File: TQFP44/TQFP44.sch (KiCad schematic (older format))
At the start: 4 parts, among them J1 Conn_01x22, J2 Conn_01x22, J3 Conn_02x22_Counter_Clockwise, J4 Conn_02x22_Counter_Clockwise

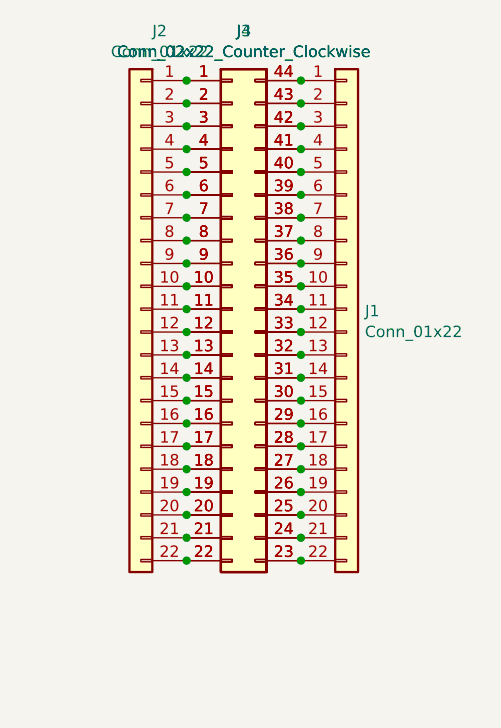
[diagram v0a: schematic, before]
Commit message: SOIC20 and SOIC28 Added
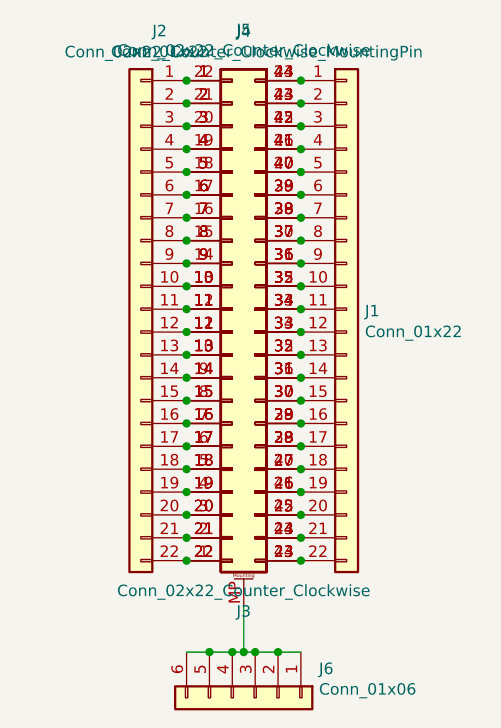
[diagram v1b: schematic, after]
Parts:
- removed J4: Conn_02x22_Counter_Clockwise, Package_DFN_QFN:QFN-44-1EP_7x7mm_P0.5mm_EP5.15x5.15mm_ThermalVias, symbol Connector_Generic:Conn_02x22_Counter_Clockwise
- added J4: Conn_02x22_Counter_Clockwise_MountingPin, Package_DFN_QFN:QFN-44-1EP_7x7mm_P0.5mm_EP5.2x5.2mm, symbol Connector_Generic_MountingPin:Conn_02x22_Counter_Clockwise_MountingPin
- added J5: Conn_02x22_Counter_Clockwise, Package_QFP:TQFP-44_10x10mm_P0.8mm, symbol Connector_Generic:Conn_02x22_Counter_Clockwise
- added J6: Conn_01x06, Connector_PinHeader_2.54mm:PinHeader_1x06_P2.54mm_Horizontal, symbol Connector_Generic:Conn_01x06
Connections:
- net at J1.1 (Pin_1), J3.44 (Pin_44): now also J4.44 (Pin_44), J5.23 (Pin_23)
- net at J1.10 (Pin_10), J3.35 (Pin_35): now also J4.35 (Pin_35), J5.32 (Pin_32)
- net at J1.11 (Pin_11), J3.34 (Pin_34): now also J4.34 (Pin_34), J5.33 (Pin_33)
- net at J1.12 (Pin_12), J3.33 (Pin_33): now also J4.33 (Pin_33), J5.34 (Pin_34)
- net at J1.13 (Pin_13), J3.32 (Pin_32): now also J4.32 (Pin_32), J5.35 (Pin_35)
- net at J1.14 (Pin_14), J3.31 (Pin_31): now also J4.31 (Pin_31), J5.36 (Pin_36)
- net at J1.15 (Pin_15), J3.30 (Pin_30): now also J4.30 (Pin_30), J5.37 (Pin_37)
- net at J1.16 (Pin_16), J3.29 (Pin_29): now also J4.29 (Pin_29), J5.38 (Pin_38)
- net at J1.17 (Pin_17), J3.28 (Pin_28): now also J4.28 (Pin_28), J5.39 (Pin_39)
- net at J1.18 (Pin_18), J3.27 (Pin_27): now also J4.27 (Pin_27), J5.40 (Pin_40)
- net at J1.19 (Pin_19), J3.26 (Pin_26): now also J4.26 (Pin_26), J5.41 (Pin_41)
- net at J1.2 (Pin_2), J3.43 (Pin_43): now also J4.43 (Pin_43), J5.24 (Pin_24)
- net at J1.20 (Pin_20), J3.25 (Pin_25): now also J4.25 (Pin_25), J5.42 (Pin_42)
- net at J1.21 (Pin_21), J3.24 (Pin_24): now also J4.24 (Pin_24), J5.43 (Pin_43)
- net at J1.22 (Pin_22), J3.23 (Pin_23): now also J4.23 (Pin_23), J5.44 (Pin_44)
- net at J1.3 (Pin_3), J3.42 (Pin_42): now also J4.42 (Pin_42), J5.25 (Pin_25)
- net at J1.4 (Pin_4), J3.41 (Pin_41): now also J4.41 (Pin_41), J5.26 (Pin_26)
- net at J1.5 (Pin_5), J3.40 (Pin_40): now also J4.40 (Pin_40), J5.27 (Pin_27)
- net at J1.6 (Pin_6), J3.39 (Pin_39): now also J4.39 (Pin_39), J5.28 (Pin_28)
- net at J1.7 (Pin_7), J3.38 (Pin_38): now also J4.38 (Pin_38), J5.29 (Pin_29)
- net at J1.8 (Pin_8), J3.37 (Pin_37): now also J4.37 (Pin_37), J5.30 (Pin_30)
- net at J1.9 (Pin_9), J3.36 (Pin_36): now also J4.36 (Pin_36), J5.31 (Pin_31)
- net at J2.1 (Pin_1), J3.1 (Pin_1): now also J4.1 (Pin_1), J5.22 (Pin_22)
- net at J2.10 (Pin_10), J3.10 (Pin_10): now also J4.10 (Pin_10), J5.13 (Pin_13)
- net at J2.11 (Pin_11), J3.11 (Pin_11): now also J4.11 (Pin_11), J5.12 (Pin_12)
- net at J2.12 (Pin_12), J3.12 (Pin_12): now also J4.12 (Pin_12), J5.11 (Pin_11)
- net at J2.13 (Pin_13), J3.13 (Pin_13): now also J4.13 (Pin_13), J5.10 (Pin_10)
- net at J2.14 (Pin_14), J3.14 (Pin_14): now also J4.14 (Pin_14), J5.9 (Pin_9)
- net at J2.15 (Pin_15), J3.15 (Pin_15): now also J4.15 (Pin_15), J5.8 (Pin_8)
- net at J2.16 (Pin_16), J3.16 (Pin_16): now also J4.16 (Pin_16), J5.7 (Pin_7)
- net at J2.17 (Pin_17), J3.17 (Pin_17): now also J4.17 (Pin_17), J5.6 (Pin_6)
- net at J2.18 (Pin_18), J3.18 (Pin_18): now also J4.18 (Pin_18), J5.5 (Pin_5)
- net at J2.19 (Pin_19), J3.19 (Pin_19): now also J4.19 (Pin_19), J5.4 (Pin_4)
- net at J2.2 (Pin_2), J3.2 (Pin_2): now also J4.2 (Pin_2), J5.21 (Pin_21)
- net at J2.20 (Pin_20), J3.20 (Pin_20): now also J4.20 (Pin_20), J5.3 (Pin_3)
- net at J2.21 (Pin_21), J3.21 (Pin_21): now also J4.21 (Pin_21), J5.2 (Pin_2)
- net at J2.22 (Pin_22), J3.22 (Pin_22): now also J4.22 (Pin_22), J5.1 (Pin_1)
- net at J2.3 (Pin_3), J3.3 (Pin_3): now also J4.3 (Pin_3), J5.20 (Pin_20)
- net at J2.4 (Pin_4), J3.4 (Pin_4): now also J4.4 (Pin_4), J5.19 (Pin_19)
- net at J2.5 (Pin_5), J3.5 (Pin_5): now also J4.5 (Pin_5), J5.18 (Pin_18)
- net at J2.6 (Pin_6), J3.6 (Pin_6): now also J4.6 (Pin_6), J5.17 (Pin_17)
- net at J2.7 (Pin_7), J3.7 (Pin_7): now also J4.7 (Pin_7), J5.16 (Pin_16)
- net at J2.8 (Pin_8), J3.8 (Pin_8): now also J4.8 (Pin_8), J5.15 (Pin_15)
- net at J2.9 (Pin_9), J3.9 (Pin_9): now also J4.9 (Pin_9), J5.14 (Pin_14)
- new net: J4.MP (MountPin), J6.1 (Pin_1), J6.2 (Pin_2), J6.3 (Pin_3), J6.4 (Pin_4), J6.5 (Pin_5), J6.6 (Pin_6)
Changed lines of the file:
@@
-$EndComp
-$Comp
-L Connector_Generic:Conn_02x22_Counter_Clockwise J3
-U 1 1 5D218126
-P 5300 3850
-F 0 "J3" H 5350 5067 50  0000 C CNN
-F 1 "Conn_02x22_Counter_Clockwise" H 5350 4976 50  0000 C CNN
-F 2 "Package_QFP:TQFP-44_10x10mm_P0.8mm" H 5300 3850 50  0001 C CNN
-F 3 "~" H 5300 3850 50  0001 C CNN
-	1    5300 3850
-	1    0    0    -1
 $EndComp
 $Comp
@@
 $EndComp
 $Comp
-L Connector_Generic:Conn_02x22_Counter_Clockwise J4
-U 1 1 5D223DAF
+L Connector_Generic:Conn_02x22_Counter_Clockwise J5
+U 1 1 5D30EF53
+P 5300 3950
+F 0 "J5" H 5350 2628 50  0000 C CNN
+F 1 "Conn_02x22_Counter_Clockwise" H 5350 2718 50  0000 C CNN
+F 2 "Package_QFP:TQFP-44_10x10mm_P0.8mm" H 5300 3950 50  0001 C CNN
+F 3 "~" H 5300 3950 50  0001 C CNN
+	1    5300 3950
+	1    0    0    1
+$EndComp
+$Comp
+L Connector_Generic:Conn_02x22_Counter_Clockwise J3
+U 1 1 5D2DB143
 P 5300 3850
-F 0 "J4" H 5350 5067 50  0000 C CNN
-F 1 "Conn_02x22_Counter_Clockwise" H 5350 4976 50  0000 C CNN
-F 2 "Package_DFN_QFN:QFN-44-1EP_7x7mm_P0.5mm_EP5.15x5.15mm_ThermalVias" H 5300 3850 50  0001 C CNN
+F 0 "J3" H 5350 2528 50  0000 C CNN
+F 1 "Conn_02x22_Counter_Clockwise" H 5350 2618 50  0000 C CNN
+F 2 "Package_QFP:TQFP-44_10x10mm_P0.8mm" H 5300 3850 50  0001 C CNN
+F 3 "~" H 5300 3850 50  0001 C CNN
+	1    5300 3850
+	1    0    0    -1
+$EndComp
+$Comp
+L Connector_Generic_MountingPin:Conn_02x22_Counter_Clockwise_MountingPin J4
+U 1 1 5D32F516
+P 5300 3850
+F 0 "J4" H 5350 5065 50  0000 C CNN
+F 1 "Conn_02x22_Counter_Clockwise_MountingPin" H 5350 4975 50  0000 C CNN
+F 2 "Package_DFN_QFN:QFN-44-1EP_7x7mm_P0.5mm_EP5.2x5.2mm" H 5300 3850 50  0001 C CNN
 F 3 "~" H 5300 3850 50  0001 C CNN
 	1    5300 3850
@@
 Connection ~ 5600 4850
 Connection ~ 5600 4950
+$Comp
+L Connector_Generic:Conn_01x06 J6
+U 1 1 5D343C09
+P 5400 5550
+F 0 "J6" V 5273 5829 50  0000 L CNN
+F 1 "Conn_01x06" V 5363 5829 50  0000 L CNN
+F 2 "Connector_PinHeader_2.54mm:PinHeader_1x06_P2.54mm_Horizontal" H 5400 5550 50  0001 C CNN
+F 3 "~" H 5400 5550 50  0001 C CNN
+	1    5400 5550
+	0    1    1    0
+$EndComp
+Wire Wire Line
+	5350 5150 5350 5350
+Wire Wire Line
+	5350 5350 5400 5350
+Connection ~ 5400 5350
+Wire Wire Line
+	5400 5350 5500 5350
+Connection ~ 5500 5350
+Wire Wire Line
+	5500 5350 5600 5350
+Wire Wire Line
+	5100 5350 5200 5350
+Connection ~ 5350 5350
+Connection ~ 5200 5350
+Wire Wire Line
+	5200 5350 5300 5350
+Connection ~ 5300 5350
+Wire Wire Line
+	5300 5350 5350 5350
 $EndSCHEMATC

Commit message: Final Revisions
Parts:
- removed J4: Conn_02x22_Counter_Clockwise_MountingPin, Package_DFN_QFN:QFN-44-1EP_7x7mm_P0.5mm_EP5.2x5.2mm, symbol Connector_Generic_MountingPin:Conn_02x22_Counter_Clockwise_MountingPin
- added J4: Conn_02x22_Counter_Clockwise, Package_DFN_QFN:QFN-44-1EP_7x7mm_P0.5mm_EP5.15x5.15mm, symbol Connector_Generic:Conn_02x22_Counter_Clockwise
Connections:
- net at J1.1 (Pin_1), J3.44 (Pin_44), J5.23 (Pin_23): now also J4.44 (Pin_44)
- net at J1.10 (Pin_10), J3.35 (Pin_35), J5.32 (Pin_32): now also J4.35 (Pin_35)
- net at J1.11 (Pin_11), J3.34 (Pin_34), J5.33 (Pin_33): now also J4.34 (Pin_34)
- net at J1.12 (Pin_12), J3.33 (Pin_33), J5.34 (Pin_34): now also J4.33 (Pin_33)
- net at J1.13 (Pin_13), J3.32 (Pin_32), J5.35 (Pin_35): now also J4.32 (Pin_32)
- net at J1.14 (Pin_14), J3.31 (Pin_31), J5.36 (Pin_36): now also J4.31 (Pin_31)
- net at J1.15 (Pin_15), J3.30 (Pin_30), J5.37 (Pin_37): now also J4.30 (Pin_30)
- net at J1.16 (Pin_16), J3.29 (Pin_29), J5.38 (Pin_38): now also J4.29 (Pin_29)
- net at J1.17 (Pin_17), J3.28 (Pin_28), J5.39 (Pin_39): now also J4.28 (Pin_28)
- net at J1.18 (Pin_18), J3.27 (Pin_27), J5.40 (Pin_40): now also J4.27 (Pin_27)
- net at J1.19 (Pin_19), J3.26 (Pin_26), J5.41 (Pin_41): now also J4.26 (Pin_26)
- net at J1.2 (Pin_2), J3.43 (Pin_43), J5.24 (Pin_24): now also J4.43 (Pin_43)
- net at J1.20 (Pin_20), J3.25 (Pin_25), J5.42 (Pin_42): now also J4.25 (Pin_25)
- net at J1.21 (Pin_21), J3.24 (Pin_24), J5.43 (Pin_43): now also J4.24 (Pin_24)
- net at J1.22 (Pin_22), J3.23 (Pin_23), J5.44 (Pin_44): now also J4.23 (Pin_23)
- net at J1.3 (Pin_3), J3.42 (Pin_42), J5.25 (Pin_25): now also J4.42 (Pin_42)
- net at J1.4 (Pin_4), J3.41 (Pin_41), J5.26 (Pin_26): now also J4.41 (Pin_41)
- net at J1.5 (Pin_5), J3.40 (Pin_40), J5.27 (Pin_27): now also J4.40 (Pin_40)
- net at J1.6 (Pin_6), J3.39 (Pin_39), J5.28 (Pin_28): now also J4.39 (Pin_39)
- net at J1.7 (Pin_7), J3.38 (Pin_38), J5.29 (Pin_29): now also J4.38 (Pin_38)
- net at J1.8 (Pin_8), J3.37 (Pin_37), J5.30 (Pin_30): now also J4.37 (Pin_37)
- net at J1.9 (Pin_9), J3.36 (Pin_36), J5.31 (Pin_31): now also J4.36 (Pin_36)
- net at J2.1 (Pin_1), J3.1 (Pin_1), J5.22 (Pin_22): now also J4.1 (Pin_1)
- net at J2.10 (Pin_10), J3.10 (Pin_10), J5.13 (Pin_13): now also J4.10 (Pin_10)
- net at J2.11 (Pin_11), J3.11 (Pin_11), J5.12 (Pin_12): now also J4.11 (Pin_11)
- net at J2.12 (Pin_12), J3.12 (Pin_12), J5.11 (Pin_11): now also J4.12 (Pin_12)
- net at J2.13 (Pin_13), J3.13 (Pin_13), J5.10 (Pin_10): now also J4.13 (Pin_13)
- net at J2.14 (Pin_14), J3.14 (Pin_14), J5.9 (Pin_9): now also J4.14 (Pin_14)
- net at J2.15 (Pin_15), J3.15 (Pin_15), J5.8 (Pin_8): now also J4.15 (Pin_15)
- net at J2.16 (Pin_16), J3.16 (Pin_16), J5.7 (Pin_7): now also J4.16 (Pin_16)
- net at J2.17 (Pin_17), J3.17 (Pin_17), J5.6 (Pin_6): now also J4.17 (Pin_17)
- net at J2.18 (Pin_18), J3.18 (Pin_18), J5.5 (Pin_5): now also J4.18 (Pin_18)
- net at J2.19 (Pin_19), J3.19 (Pin_19), J5.4 (Pin_4): now also J4.19 (Pin_19)
- net at J2.2 (Pin_2), J3.2 (Pin_2), J5.21 (Pin_21): now also J4.2 (Pin_2)
- net at J2.20 (Pin_20), J3.20 (Pin_20), J5.3 (Pin_3): now also J4.20 (Pin_20)
- net at J2.21 (Pin_21), J3.21 (Pin_21), J5.2 (Pin_2): now also J4.21 (Pin_21)
- net at J2.22 (Pin_22), J3.22 (Pin_22), J5.1 (Pin_1): now also J4.22 (Pin_22)
- net at J2.3 (Pin_3), J3.3 (Pin_3), J5.20 (Pin_20): now also J4.3 (Pin_3)
- net at J2.4 (Pin_4), J3.4 (Pin_4), J5.19 (Pin_19): now also J4.4 (Pin_4)
- net at J2.5 (Pin_5), J3.5 (Pin_5), J5.18 (Pin_18): now also J4.5 (Pin_5)
- net at J2.6 (Pin_6), J3.6 (Pin_6), J5.17 (Pin_17): now also J4.6 (Pin_6)
- net at J2.7 (Pin_7), J3.7 (Pin_7), J5.16 (Pin_16): now also J4.7 (Pin_7)
- net at J2.8 (Pin_8), J3.8 (Pin_8), J5.15 (Pin_15): now also J4.8 (Pin_8)
- net at J2.9 (Pin_9), J3.9 (Pin_9), J5.14 (Pin_14): now also J4.9 (Pin_9)
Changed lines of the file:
@@
-	1    0    0    -1
-$EndComp
-$Comp
-L Connector_Generic_MountingPin:Conn_02x22_Counter_Clockwise_MountingPin J4
-U 1 1 5D32F516
-P 5300 3850
-F 0 "J4" H 5350 5065 50  0000 C CNN
-F 1 "Conn_02x22_Counter_Clockwise_MountingPin" H 5350 4975 50  0000 C CNN
-F 2 "Package_DFN_QFN:QFN-44-1EP_7x7mm_P0.5mm_EP5.2x5.2mm" H 5300 3850 50  0001 C CNN
-F 3 "~" H 5300 3850 50  0001 C CNN
-	1    5300 3850
 	1    0    0    -1
 $EndComp
@@
 	0    1    1    0
 $EndComp
-Wire Wire Line
-	5350 5150 5350 5350
-Wire Wire Line
-	5350 5350 5400 5350
 Connection ~ 5400 5350
 Wire Wire Line
@@
 Wire Wire Line
 	5100 5350 5200 5350
-Connection ~ 5350 5350
 Connection ~ 5200 5350
 Wire Wire Line
@@
 Connection ~ 5300 5350
 Wire Wire Line
-	5300 5350 5350 5350
+	5300 5350 5400 5350
+$Comp
+L Connector_Generic:Conn_02x22_Counter_Clockwise J4
+U 1 1 5D472302
+P 5300 3850
+F 0 "J4" H 5350 2528 50  0000 C CNN
+F 1 "Conn_02x22_Counter_Clockwise" H 5350 2618 50  0000 C CNN
+F 2 "Package_DFN_QFN:QFN-44-1EP_7x7mm_P0.5mm_EP5.15x5.15mm" H 5300 3850 50  0001 C CNN
+F 3 "~" H 5300 3850 50  0001 C CNN
+	1    5300 3850
+	1    0    0    -1
+$EndComp
 $EndSCHEMATC
